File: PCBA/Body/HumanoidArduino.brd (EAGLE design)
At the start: 100 x 65 mm, 88 parts, among them IC1 7805TV, J2 22-27-2041-04, Q1 12MHz, U4 CH340G, U5 SX1308_B628, X1 MINI-USB-UX60-MB-5S8

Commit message: PCBA again
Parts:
- removed F25, F26: POLYSWITCH, HumanoidLbr:1206
- removed JP26, JP27: JUMPER_3X1_0.1, HumanoidLbr:CONN_3X1_0.1"
- removed R2: (no value), SparkFun-Resistors:0603-ARV
- added C5: 22u, capacitor-wima:C2.5-3
- added U6: MCP73213-A6SI/MF, DFN300X300X100-11N:DFN300X300X100-11N
- C4: value 22p -> 22u
- L1: value (none) -> 15uH
- R1: value (none) -> 10k; device SparkFun-Resistors:0603-ARV -> SparkFun-Passives:0805
- R11: value 670R -> 18k
- R12: value 670R -> 1k
- moved R1 132.5 mm to (-6.35, -53.3), turned to 0 degrees
- moved L1 107.6 mm to (45.7, 33.0), turned to 180 degrees
- moved D1 96.7 mm to (39.4, 30.5), turned to 180 degrees
- moved C4 91.5 mm to (38.1, 40.6), turned to 180 degrees
- moved R12 83.1 mm to (41.9, 34.3), turned to 90 degrees
- moved U5 82.4 mm to (45.7, 36.8)
- moved R11 78.6 mm to (38.1, 34.3)
- moved C1 47.7 mm to (25.4, 2.54), turned to 180 degrees
- moved U4 14.2 mm to (54.6, 35.6), turned to 270 degrees
- moved C3 13.7 mm to (48.3, 45.7)
- moved C2 11.7 mm to (53.3, 45.7)
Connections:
- removed net N$51: F25.P$1, JP26.P$2
- removed net N$52: F26.P$1, JP27.P$2
- new net N$62: U6.2
- new net N$63: U6.4
- new net N$64: R1.2, U6.10
- net +5V: no longer F25.P$2, F26.P$2
- net GND: now also C5.2, JP10.P$3, JP11.P$3, JP12.P$3, JP13.P$3, JP14.P$3, JP15.P$3, JP16.P$3, JP17.P$3, JP5.P$3, JP6.P$3, JP7.P$3, JP8.P$3, R1.1, U6.9; no longer JP26.P$3, JP27.P$3
- net N$59: now also R11.1
- net PWM12: no longer R3.8
- net PWM13: no longer R3.7
- net PWM14: no longer R3.6
- net PWM15: no longer R3.5
- net PWM22: now also R10.2
- net PWM24: now also R3.5
- net PWM25: now also R3.6
- net PWM26: now also R3.7
- net PWM27: now also R3.8
- net V-CHG: now also C5.1

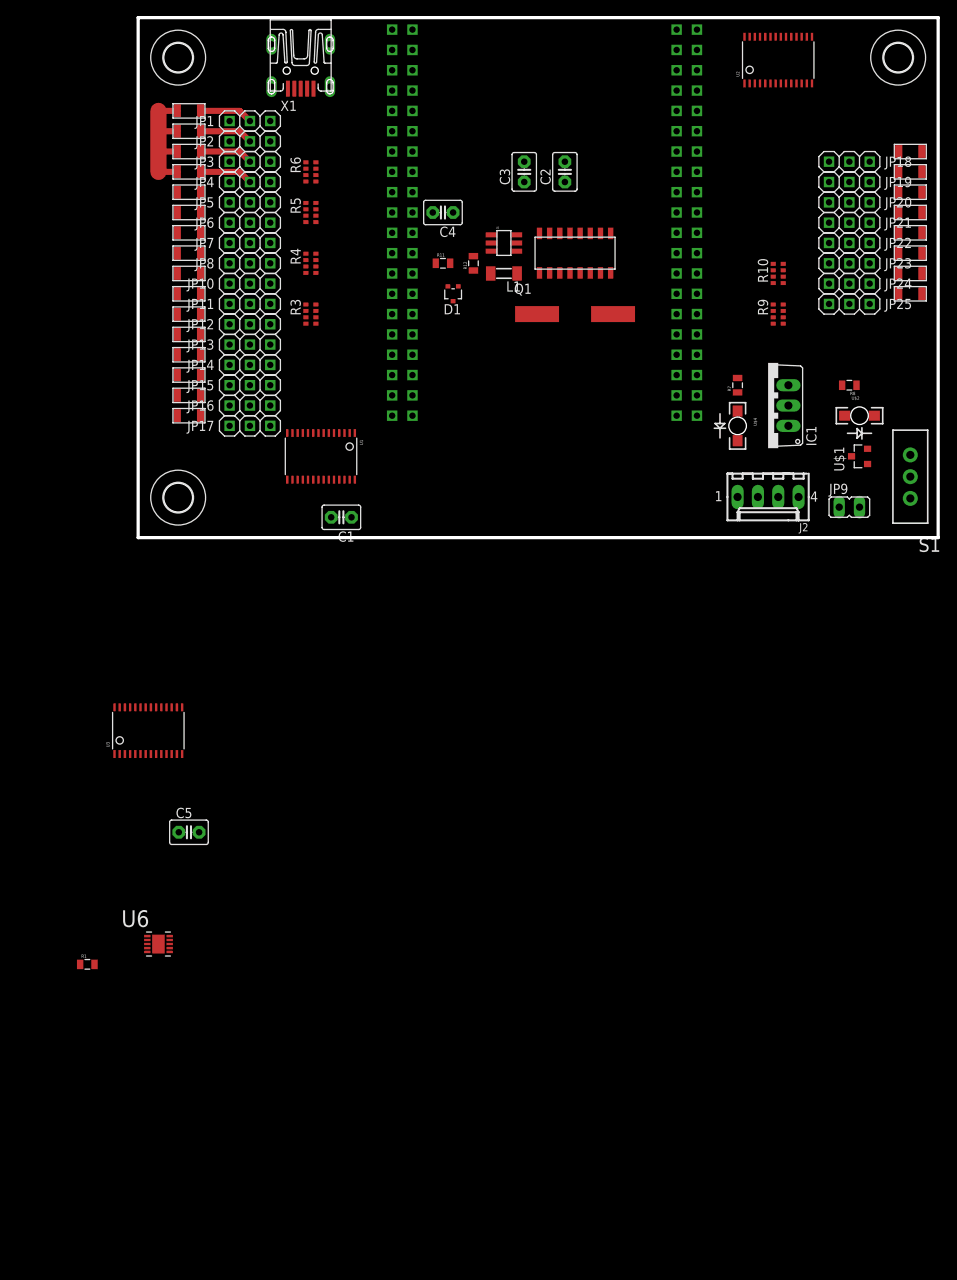
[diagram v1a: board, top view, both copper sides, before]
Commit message: Using proper 5V buck reg
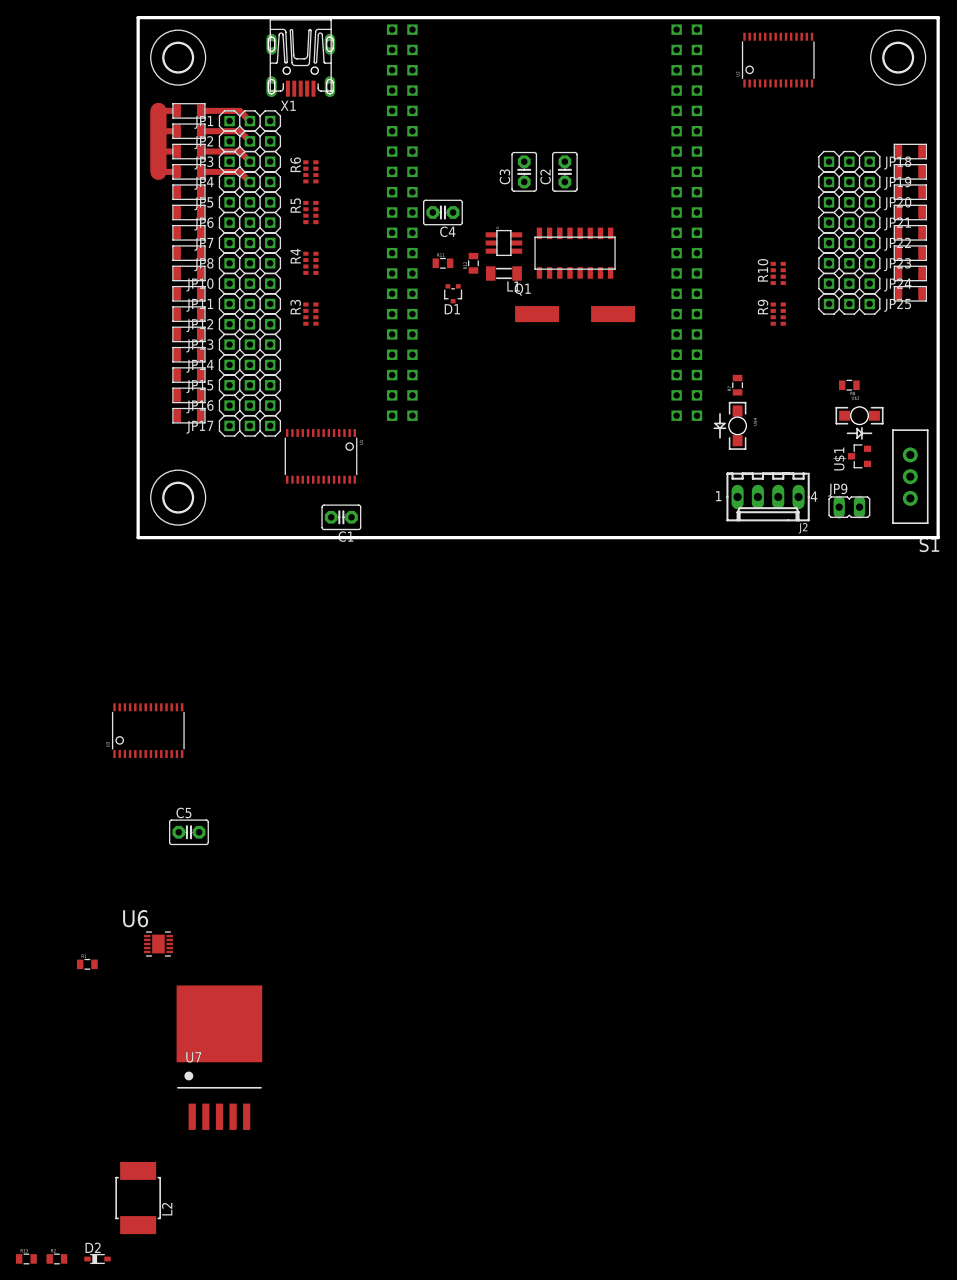
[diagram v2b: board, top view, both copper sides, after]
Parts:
- removed IC1: 7805TV, linear:TO220V
- added D2: 5V5, diode:SOD323_ST
- added L2: 22uH, inductor-neosid:MS85
- added R13: 3K, SparkFun-Passives:0805
- added R2: 1K, SparkFun-Passives:0805
- added U7: AP1501A, TO-263-5:TO-263-5
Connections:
- new net N$65: R13.2, R2.1, U7.4
- new net N$66: D2.C, L2.1, R13.1, U7.2
- net +5V: now also L2.2; no longer IC1.3
- net 8.4V: now also U7.1; no longer IC1.1
- net GND: now also D2.A, R2.2, U7.5, U7.TAB; no longer IC1.2
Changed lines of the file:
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@@
 <element name="H3" library="holes" package="3,6" value="MOUNT-HOLE3.6" x="95" y="60"/>
 <element name="U$3" library="ZMZE" package="CHIP" value="CHIP" x="31.75" y="63.5" rot="MR180"/>
-<element name="IC1" library="linear" package="TO220V" value="7805TV" x="78.74" y="16.51" rot="R90"/>
 <element name="U1" library="adafruit" package="TSSOP28" value="" x="22.86" y="10.16" rot="R180"/>
 <element name="U2" library="adafruit" package="TSSOP28" value="" x="80.01" y="59.69"/>
@@
 <element name="U6" library="DFN300X300X100-11N" package="DFN300X300X100-11N" value="MCP73213-A6SI/MF" x="2.54" y="-50.8"/>
 <element name="R1" library="SparkFun-Passives" package="0805" value="10k" x="-6.35" y="-53.34"/>
+<element name="U7" library="TO-263-5" package="TO-263-5" value="AP1501A" x="10.16" y="-72.39"/>
+<element name="L2" library="inductor-neosid" package="MS85" value="22uH" x="0" y="-82.55">
+<attribute name="MF" value="" x="0" y="-82.55" size="1.778" layer="27" display="off"/>
+<attribute name="MPN" value="" x="0" y="-82.55" size="1.778" layer="27" display="off"/>
+<attribute name="OC_NEWARK" value="unknown" x="0" y="-82.55" size="1.778" layer="27" display="off"/>
+<attribute name="OC_FARNELL" value="unknown" x="0" y="-82.55" size="1.778" layer="27" display="off"/>
+</element>
+<element name="D2" library="diode" package="SOD323_ST" value="5V5" x="-5.08" y="-90.17"/>
+<element name="R2" library="SparkFun-Passives" package="0805" value="1K" x="-10.16" y="-90.17"/>
+<element name="R13" library="SparkFun-Passives" package="0805" value="3K" x="-13.97" y="-90.17"/>
 </elements>
 <signals>
 <signal name="GND" airwireshidden="yes">
-<contactref element="IC1" pad="2"/>
 <contactref element="J2" pad="1"/>
 <contactref element="U$3" pad="GND@0"/>
@@
 <contactref element="U6" pad="9"/>
 <contactref element="R1" pad="1"/>
+<contactref element="D2" pad="A"/>
+<contactref element="R2" pad="2"/>
+<contactref element="U7" pad="TAB"/>
+<contactref element="U7" pad="5"/>
 <wire x1="78.385" y1="56.7722" x2="84.235" y2="56.7722" width="0" layer="19" extent="1-1"/>
 <wire x1="77.735" y1="56.7722" x2="78.385" y2="56.7722" width="0" layer="19" extent="1-1"/>
@@
 <wire x1="91.17" y1="9.21" x2="92.02" y2="15.24" width="0" layer="19" extent="1-1"/>
 <wire x1="87.63" y1="3.81" x2="91.17" y2="9.21" width="0" layer="19" extent="1-1"/>
-<wire x1="81.28" y1="16.51" x2="92.02" y2="15.24" width="0" layer="19" extent="1-1"/>
-<wire x1="74.93" y1="12.12" x2="81.28" y2="16.51" width="0" layer="19" extent="1-1"/>
-<wire x1="74.93" y1="5.08" x2="74.93" y2="12.12" width="0" layer="19" extent="1-1"/>
+<wire x1="74.93" y1="5.08" x2="87.63" y2="3.81" width="0" layer="19" extent="1-1"/>
+<wire x1="74.93" y1="12.12" x2="74.93" y2="5.08" width="0" layer="19" extent="1-1"/>
 <wire x1="67.31" y1="15.24" x2="74.93" y2="12.12" width="0" layer="19" extent="1-1"/>
 <wire x1="69.85" y1="40.64" x2="75.785" y2="56.7722" width="0" layer="19" extent="1-1"/>
@@
 <wire x1="3.937" y1="-50.292" x2="7.62" y2="-36.83" width="0" layer="19" extent="1-1"/>
 <wire x1="-7.25" y1="-53.34" x2="3.937" y2="-50.292" width="0" layer="19" extent="1-1"/>
+<wire x1="10.16" y1="-60.774" x2="3.937" y2="-50.292" width="0" layer="19" extent="1-1"/>
+<wire x1="13.56" y1="-72.39" x2="10.16" y2="-60.774" width="0" layer="19" extent="1-1"/>
+<wire x1="-3.83" y1="-90.17" x2="13.56" y2="-72.39" width="0" layer="19" extent="1-1"/>
+<wire x1="-9.26" y1="-90.17" x2="-3.83" y2="-90.17" width="0" layer="19" extent="1-1"/>
 </signal>
 <signal name="\O\E">
@@
 </signal>
 <signal name="8.4V">
-<contactref element="IC1" pad="1"/>
 <contactref element="U$1" pad="3"/>
 <contactref element="R7" pad="2"/>
-<wire x1="89.17" y1="10.16" x2="81.28" y2="13.97" width="0" layer="19" extent="1-1"/>
+<contactref element="U7" pad="1"/>
 <wire x1="74.93" y1="19.95" x2="89.17" y2="10.16" width="0" layer="19" extent="1-1"/>
+<wire x1="6.76" y1="-72.39" x2="74.93" y2="19.95" width="0" layer="19" extent="1-1"/>
 </signal>
 <signal name="4.2V_CHG">
@@
 </signal>
 <signal name="+5V">
-<contactref element="IC1" pad="3"/>
 <contactref element="U$3" pad="CHG-IN"/>
 <contactref element="U1" pad="28"/>
@@
 <contactref element="F15" pad="P$2"/>
 <contactref element="F16" pad="P$2"/>
+<contactref element="L2" pad="2"/>
 <wire x1="97.97" y1="45.72" x2="97.97" y2="48.26" width="0" layer="19" extent="1-1"/>
 <wire x1="97.97" y1="43.18" x2="97.97" y2="45.72" width="0" layer="19" extent="1-1"/>
@@
 <wire x1="97.97" y1="30.48" x2="97.97" y2="33.02" width="0" layer="19" extent="1-1"/>
 <wire x1="88" y1="19.05" x2="97.97" y2="30.48" width="0" layer="19" extent="1-1"/>
-<wire x1="81.28" y1="19.05" x2="88" y2="19.05" width="0" layer="19" extent="1-1"/>
 <wire x1="76.435" y1="56.7722" x2="97.97" y2="48.26" width="0" layer="19" extent="1-1"/>
 <wire x1="75.785" y1="62.6078" x2="76.435" y2="56.7722" width="0" layer="19" extent="1-1"/>
-<wire x1="59.055" y1="33.085" x2="81.28" y2="19.05" width="0" layer="19" extent="1-1"/>
+<wire x1="59.055" y1="33.085" x2="76.435" y2="56.7722" width="0" layer="19" extent="1-1"/>
 <wire x1="34.29" y1="15.24" x2="59.055" y2="33.085" width="0" layer="19" extent="1-1"/>
 <wire x1="27.085" y1="13.0778" x2="34.29" y2="15.24" width="0" layer="19" extent="1-1"/>
@@
 <wire x1="4.9" y1="48.26" x2="4.9" y2="45.72" width="0" layer="19" extent="1-1"/>
 <wire x1="21.92" y1="56.12" x2="4.9" y2="53.34" width="0" layer="19" extent="1-1"/>
+<wire x1="0" y1="-79.167" x2="26.67" y2="2.54" width="0" layer="19" extent="1-1"/>
 </signal>
 <signal name="VDD">
@@
 <wire x1="3.937" y1="-49.8094" x2="-5.45" y2="-53.34" width="0" layer="19" extent="1-1"/>
 </signal>
+<signal name="N$65">
+<contactref element="U7" pad="4"/>
+<contactref element="R2" pad="1"/>
+<contactref element="R13" pad="2"/>
+<wire x1="-11.06" y1="-90.17" x2="-13.07" y2="-90.17" width="0" layer="19" extent="1-1"/>
+<wire x1="11.86" y1="-72.39" x2="-11.06" y2="-90.17" width="0" layer="19" extent="1-1"/>
+</signal>
+<signal name="N$66">
+<contactref element="R13" pad="1"/>
+<contactref element="U7" pad="2"/>
+<contactref element="L2" pad="1"/>
+<contactref element="D2" pad="C"/>
+<wire x1="-6.33" y1="-90.17" x2="-14.87" y2="-90.17" width="0" layer="19" extent="1-1"/>
+<wire x1="0" y1="-85.933" x2="-6.33" y2="-90.17" width="0" layer="19" extent="1-1"/>
+<wire x1="8.46" y1="-72.39" x2="0" y2="-85.933" width="0" layer="19" extent="1-1"/>
+</signal>
 </signals>

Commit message: selected a few more parts for the PCB
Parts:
- removed U3: (no value), adafruit:TSSOP28
- L1: value 15uH -> 22uH; device inductor-neosid:SM-1206 -> inductor-neosid:MS85
- moved R13 137.4 mm to (81.3, 8.89)
- moved R2 136.5 mm to (83.8, 8.89), turned to 270 degrees
- moved L2 133.9 mm to (73.7, 29.2)
- moved R1 126.8 mm to (45.7, 62.2)
- moved D2 126.5 mm to (73.7, 8.89)
- moved U6 117.0 mm to (44.5, 58.4)
- moved U7 111.7 mm to (82.5, 12.7)
- moved C5 77.3 mm to (44.5, 30.5), turned to 90 degrees
- moved R9 14.0 mm to (80.0, 41.9)
- moved L1 10.9 mm to (41.9, 22.9), turned to 90 degrees
- moved F17 3.81 mm to (96.5, 52.1)
- moved F18 3.81 mm to (96.5, 49.5)
- moved F19 3.81 mm to (96.5, 47.0)
- moved F20 3.81 mm to (96.5, 44.5)
- moved JP20 3.81 mm to (88.9, 45.7)
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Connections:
- removed net VDD: U3.28
- net GND: no longer U3.14

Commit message: working on PCBA
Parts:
- added LED1: (no value), led:SML1206
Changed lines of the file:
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@@
 <attribute name="OC_FARNELL" value="unknown" x="41.91" y="22.86" size="1.778" layer="27" rot="R90" display="off"/>
 </element>
+<element name="LED1" library="led" package="SML1206" value="" x="5.08" y="-8.89"/>
 </elements>
 <signals>
